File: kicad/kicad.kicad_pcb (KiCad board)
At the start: 4 copper layers, 31.8 x 37.3 mm, 90 parts, among them J201 USB_C_Receptacle_USB2.0_16P, J301 BATTERY_CONN, J501 MOTOR_CONN, Q401 Si1308EDL, Q701 DMG1012T, SW101 PWR_SWITCH, SW601 BT1, SW602 BT3, SW603 BT2, SW604 BT4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

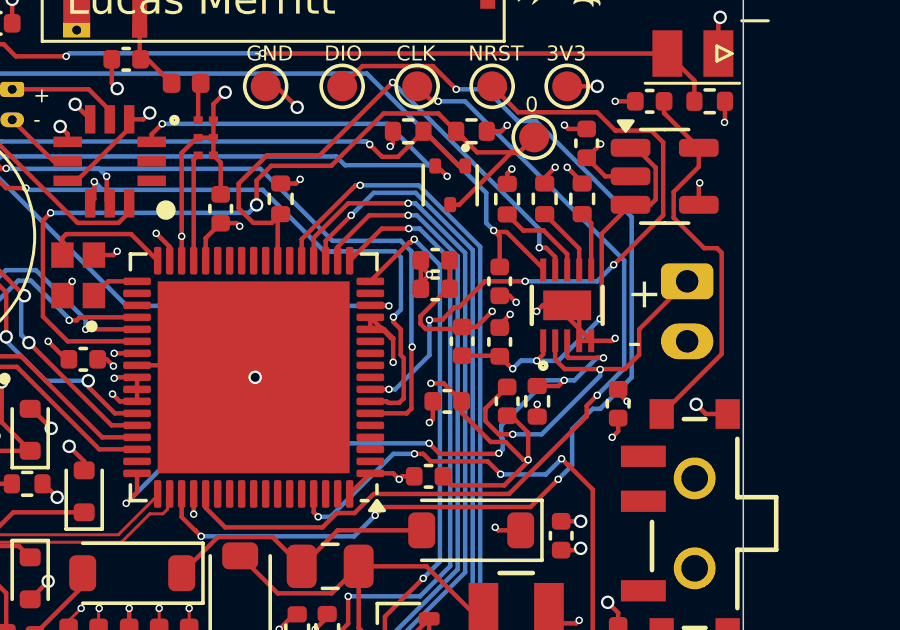
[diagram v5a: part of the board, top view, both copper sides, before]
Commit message: Update BOOT0
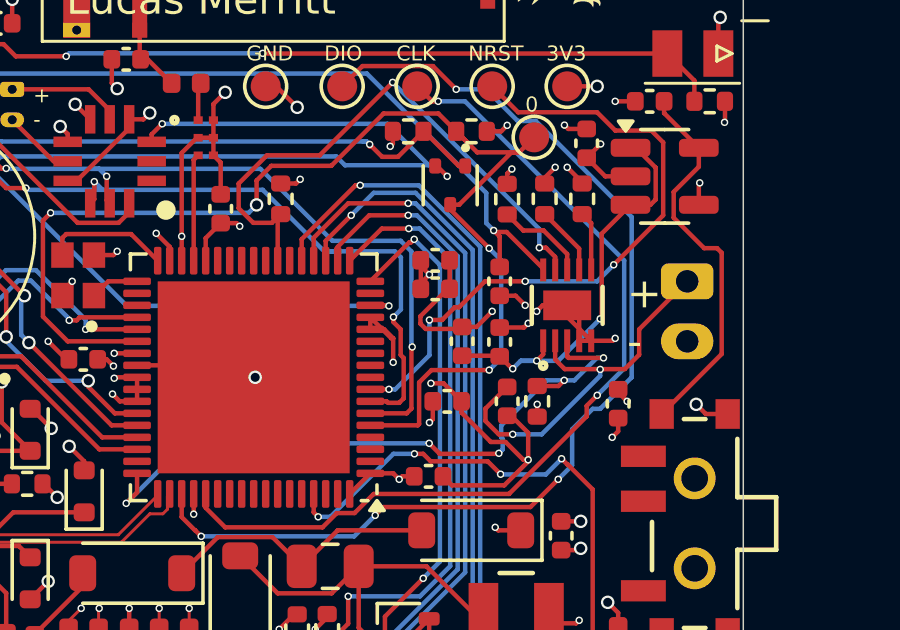
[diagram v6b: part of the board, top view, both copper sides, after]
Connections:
- U702 pad 40: Net-(Q701-D) -> unconnected-(U702-PE4-Pad40)
- U702 pad 5: unconnected-(U702-PH3-Pad5) -> Net-(Q701-D)
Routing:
- net Net-(Q701-D): track 29.4 -> 41.3 mm, vias 2 -> 4
- net GND: track 85.1 -> 85.8 mm
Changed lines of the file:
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@@
 	(net 75 "unconnected-(U702-PC14-Pad3)")
 	(net 76 "unconnected-(U702-PA1-Pad16)")
-	(net 77 "unconnected-(U702-PH3-Pad5)")
+	(net 77 "unconnected-(U702-PE4-Pad40)")
 	(net 78 "Net-(U702-OSC_OUT)")
 	(net 79 "unconnected-(U702-PC13-Pad2)")
@@
 			(layers "F.Cu" "F.Paste" "F.Mask")
 			(roundrect_rratio 0.25)
-			(net 77 "unconnected-(U702-PH3-Pad5)")
+			(net 92 "Net-(Q701-D)")
 			(pinfunction "PH3")
 			(pintype "bidirectional")
@@
 			(layers "F.Cu" "F.Paste" "F.Mask")
 			(roundrect_rratio 0.25)
-			(net 92 "Net-(Q701-D)")
+			(net 77 "unconnected-(U702-PE4-Pad40)")
 			(pinfunction "PE4")
 			(pintype "bidirectional")
@@
 	)
 	(segment
-		(start 150.25 109.54)
-		(end 150.25 109.45)
+		(start 150.78 108.48)
+		(end 151.1 108.8)
 		(width 0.15)
 		(layer "F.Cu")
@@
 	)
 	(segment
+		(start 150.25 108.48)
+		(end 150.78 108.48)
+		(width 0.15)
+		(layer "F.Cu")
+		(net 1)
+	)
+	(segment
 		(start 140.95 105.1)
 		(end 140.95 104.042)
@@
 	)
 	(segment
+		(start 150.25 109.54)
+		(end 151.06 109.54)
+		(width 0.15)
+		(layer "F.Cu")
+		(net 1)
+	)
+	(segment
 		(start 148.931886 109.588114)
 		(end 149 109.52)
@@
 	)
 	(segment
-		(start 150.25 108.48)
-		(end 150.58 108.48)
-		(width 0.15)
-		(layer "F.Cu")
-		(net 1)
-	)
-	(segment
 		(start 157.85 119.72248)
 		(end 157.17752 119.72248)
@@
 	)
 	(segment
-		(start 150.25 109.45)
-		(end 150.6 109.1)
-		(width 0.15)
-		(layer "F.Cu")
-		(net 1)
-	)
-	(segment
 		(start 151.2 114.004289)
 		(end 150.404289 114.8)
@@
 	)
 	(segment
-		(start 150.58 108.48)
-		(end 150.8 108.7)
-		(width 0.15)
-		(layer "F.Cu")
-		(net 1)
-	)
-	(segment
 		(start 144.719999 122.780001)
 		(end 144.7 122.8)
@@
 	)
 	(segment
+		(start 151.06 109.54)
+		(end 151.2 109.4)
+		(width 0.15)
+		(layer "F.Cu")
+		(net 1)
+	)
+	(segment
 		(start 142.8 101.5)
 		(end 143.5 102.2)
@@
 	)
 	(via
-		(at 150.8 108.7)
-		(size 0.25)
-		(drill 0.15)
-		(layers "F.Cu" "B.Cu")
-		(net 1)
-	)
-	(via
 		(at 151.485 109)
 		(size 0.25)
@@
 	)
 	(via
-		(at 150.6 109.1)
-		(size 0.25)
-		(drill 0.15)
-		(layers "F.Cu" "B.Cu")
-		(net 1)
-	)
-	(via
 		(at 157.6 96.5)
 		(size 0.45)
@@
 	)
 	(via
+		(at 151.1 108.8)
+		(size 0.25)
+		(drill 0.15)
+		(layers "F.Cu" "B.Cu")
+		(net 1)
+	)
+	(via
 		(at 144.7 122.8)
 		(size 0.25)
@@
 	)
 	(via
+		(at 151.2 109.4)
+		(size 0.25)
+		(drill 0.15)
+		(layers "F.Cu" "B.Cu")
+		(net 1)
+	)
+	(via
 		(at 139.9 118.9)
 		(size 0.25)
@@
 	)
 	(segment
+		(start 147.565 112.756985)
+		(end 147.565 111.36875)
+		(width 0.15)
+		(layer "F.Cu")
+		(net 92)
+	)
+	(segment
+		(start 145.9375 112.8)
+		(end 147.521985 112.8)
+		(width 0.15)
+		(layer "F.Cu")
+		(net 92)
+	)
+	(segment
 		(start 150.900001 103.699999)
 		(end 150.9 103.699999)
@@
 	)
 	(segment
+		(start 148.6 105.6)
+		(end 148.6 105.445)
+		(width 0.15)
+		(layer "F.Cu")
+		(net 92)
+	)
+	(segment
+		(start 147.97504 110.95871)
+		(end 149.9 110.95871)
+		(width 0.15)
+		(layer "F.Cu")
+		(net 92)
+	)
+	(segment
 		(start 148.205 102.405)
 		(end 146.381432 102.405)
@@
 	)
 	(segment
+		(start 149.9 106.9)
+		(end 148.6 105.6)
+		(width 0.15)
+		(layer "F.Cu")
+		(net 92)
+	)
+	(segment
 		(start 135.282158 105.717842)
 		(end 135.025 105.975)
@@
 	)
 	(segment
+		(start 147.565 111.36875)
+		(end 147.97504 110.95871)
+		(width 0.15)
+		(layer "F.Cu")
+		(net 92)
+	)
+	(segment
 		(start 149.225 103.425)
 		(end 148.8 103)
@@
 		(net 92)
 	)
+	(segment
+		(start 147.521985 112.8)
+		(end 147.565 112.756985)
+		(width 0.15)
+		(layer "F.Cu")
+		(net 92)
+	)
+	(via
+		(at 149.9 106.9)
+		(size 0.25)
+		(drill 0.15)
+		(layers "F.Cu" "B.Cu")
+		(net 92)
+	)
 	(via
 		(at 135.282158 105.717842)
@@
 		(net 92)
 	)
+	(via
+		(at 149.9 110.95871)
+		(size 0.25)
+		(drill 0.15)
+		(layers "F.Cu" "B.Cu")
+		(net 92)
+	)
+	(segment
+		(start 149.9 110.95871)
+		(end 150.3 110.55871)
+		(width 0.15)
+		(layer "B.Cu")
+		(net 92)
+	)
+	(segment
+		(start 150.3 110.55871)
+		(end 150.3 107.3)
+		(width 0.15)
+		(layer "B.Cu")
+		(net 92)
+	)
+	(segment
+		(start 150.3 107.3)
+		(end 149.9 106.9)
+		(width 0.15)
+		(layer "B.Cu")
+		(net 92)
+	)

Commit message: V2.0.0
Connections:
- net REGV renamed /Battery Management/REGV
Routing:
- net Net-(Q701-D): track 41.3 -> 18.6 mm, vias 4 -> 2
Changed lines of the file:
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@@
 	(net 1 "GND")
 	(net 2 "+BATT")
-	(net 3 "REGV")
+	(net 3 "/Battery Management/REGV")
 	(net 4 "/E-Paper Display/PREVGH")
 	(net 5 "Net-(D401-A)")
@@
 			(layers "F.Cu" "F.Paste" "F.Mask")
 			(roundrect_rratio 0.25)
-			(net 3 "REGV")
+			(net 3 "/Battery Management/REGV")
 			(pintype "passive")
 		)
@@
 			(layers "F.Cu" "F.Paste" "F.Mask")
 			(roundrect_rratio 0.25)
-			(net 3 "REGV")
+			(net 3 "/Battery Management/REGV")
 			(pinfunction "OUT")
 			(pintype "power_out")
@@
 			(size 0.8128 0.9906)
 			(layers "F.Cu" "F.Paste" "F.Mask")
-			(net 3 "REGV")
+			(net 3 "/Battery Management/REGV")
 			(pinfunction "C")
 			(pintype "passive")
@@
 	)
 	(segment
-		(start 148.901432 105.445)
-		(end 148.6 105.445)
-		(width 0.15)
-		(layer "F.Cu")
-		(net 92)
-	)
-	(segment
-		(start 142.636432 104.15)
-		(end 142.146446 104.639986)
-		(width 0.15)
-		(layer "F.Cu")
-		(net 92)
-	)
-	(segment
-		(start 151.4 103.2)
-		(end 150.900001 103.699999)
+		(start 151.287853 103.2)
+		(end 149.042853 105.445)
 		(width 0.15)
 		(layer "F.Cu")
@@
 	)
 	(segment
-		(start 135.025 105.975)
-		(end 135.025 109.175)
-		(width 0.15)
-		(layer "F.Cu")
-		(net 92)
-	)
-	(segment
-		(start 149.225 103.425)
-		(end 148.205 102.405)
-		(width 0.15)
-		(layer "F.Cu")
-		(net 92)
-	)
-	(segment
-		(start 142.146446 104.639986)
-		(end 142.146446 105.453554)
+		(start 149.295 103.495)
+		(end 151.105 103.495)
 		(width 0.15)
 		(layer "F.Cu")
@@
 	)
 	(segment
-		(start 150.900001 103.699999)
-		(end 150.9 103.699999)
-		(width 0.15)
-		(layer "F.Cu")
-		(net 92)
-	)
-	(segment
-		(start 150.9 103.699999)
-		(end 150.646433 103.699999)
-		(width 0.15)
-		(layer "F.Cu")
-		(net 92)
-	)
-	(segment
-		(start 146.381432 102.405)
-		(end 144.636432 104.15)
-		(width 0.15)
-		(layer "F.Cu")
-		(net 92)
-	)
-	(segment
-		(start 149.499999 103.699999)
-		(end 149.225 103.425)
+		(start 149.042853 105.445)
+		(end 148.6 105.445)
 		(width 0.15)
 		(layer "F.Cu")
@@
 	)
 	(segment
-		(start 135.85 110)
-		(end 138.1625 110)
+		(start 151.4 103.2)
+		(end 151.287853 103.2)
 		(width 0.15)
 		(layer "F.Cu")
@@
 	)
 	(segment
-		(start 148.205 102.405)
-		(end 146.381432 102.405)
+		(start 148.8 103)
+		(end 149.295 103.495)
 		(width 0.15)
 		(layer "F.Cu")
@@
 	)
 	(segment
-		(start 135.282158 105.717842)
-		(end 135.025 105.975)
-		(width 0.15)
-		(layer "F.Cu")
-		(net 92)
-	)
-	(segment
-		(start 150.646433 103.699999)
-		(end 148.901432 105.445)
-		(width 0.15)
-		(layer "F.Cu")
-		(net 92)
-	)
-	(segment
 		(start 147.565 111.36875)
 		(end 147.97504 110.95871)
@@
 	)
 	(segment
-		(start 149.225 103.425)
-		(end 148.8 103)
-		(width 0.15)
-		(layer "F.Cu")
-		(net 92)
-	)
-	(segment
-		(start 144.636432 104.15)
-		(end 142.636432 104.15)
-		(width 0.15)
-		(layer "F.Cu")
-		(net 92)
-	)
-	(segment
-		(start 150.9 103.699999)
-		(end 149.499999 103.699999)
-		(width 0.15)
-		(layer "F.Cu")
-		(net 92)
-	)
-	(segment
-		(start 135.025 109.175)
-		(end 135.85 110)
+		(start 147.521985 112.8)
+		(end 147.565 112.756985)
 		(width 0.15)
 		(layer "F.Cu")
@@
 	)
 	(segment
-		(start 147.521985 112.8)
-		(end 147.565 112.756985)
+		(start 151.105 103.495)
+		(end 151.4 103.2)
 		(width 0.15)
 		(layer "F.Cu")
@@
 	)
 	(via
-		(at 135.282158 105.717842)
-		(size 0.25)
-		(drill 0.15)
-		(layers "F.Cu" "B.Cu")
-		(net 92)
-	)
-	(via
-		(at 142.146446 105.453554)
-		(size 0.45)
-		(drill 0.3)
-		(layers "F.Cu" "B.Cu")
-		(net 92)
-	)
-	(via
 		(at 149.9 110.95871)
 		(size 0.25)
@@
 		(width 0.15)
 		(layer "B.Cu")
-		(net 92)
-	)
-	(segment
-		(start 142.146446 105.453554)
-		(end 141.882158 105.717842)
-		(width 0.15)
-		(layer "B.Cu")
-		(net 92)
-	)
-	(segment
-		(start 141.882158 105.717842)
-		(end 135.282158 105.717842)
-		(width 0.15)
-		(layer "B.Cu")
